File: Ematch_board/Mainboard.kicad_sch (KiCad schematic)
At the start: 72 parts, among them J10 Conn_01x02_Male, J7 RBUS, J8 USB_C_Receptacle_USB2.0, J9 Conn_01x02_Male, Q1 MMDT2222A, U2 LTC4411, U3 RT9025-25GSP, U4 LTC4411, U5 SN65HVD230, U6 INTERFACE-CP2102-GMR(QFN28)

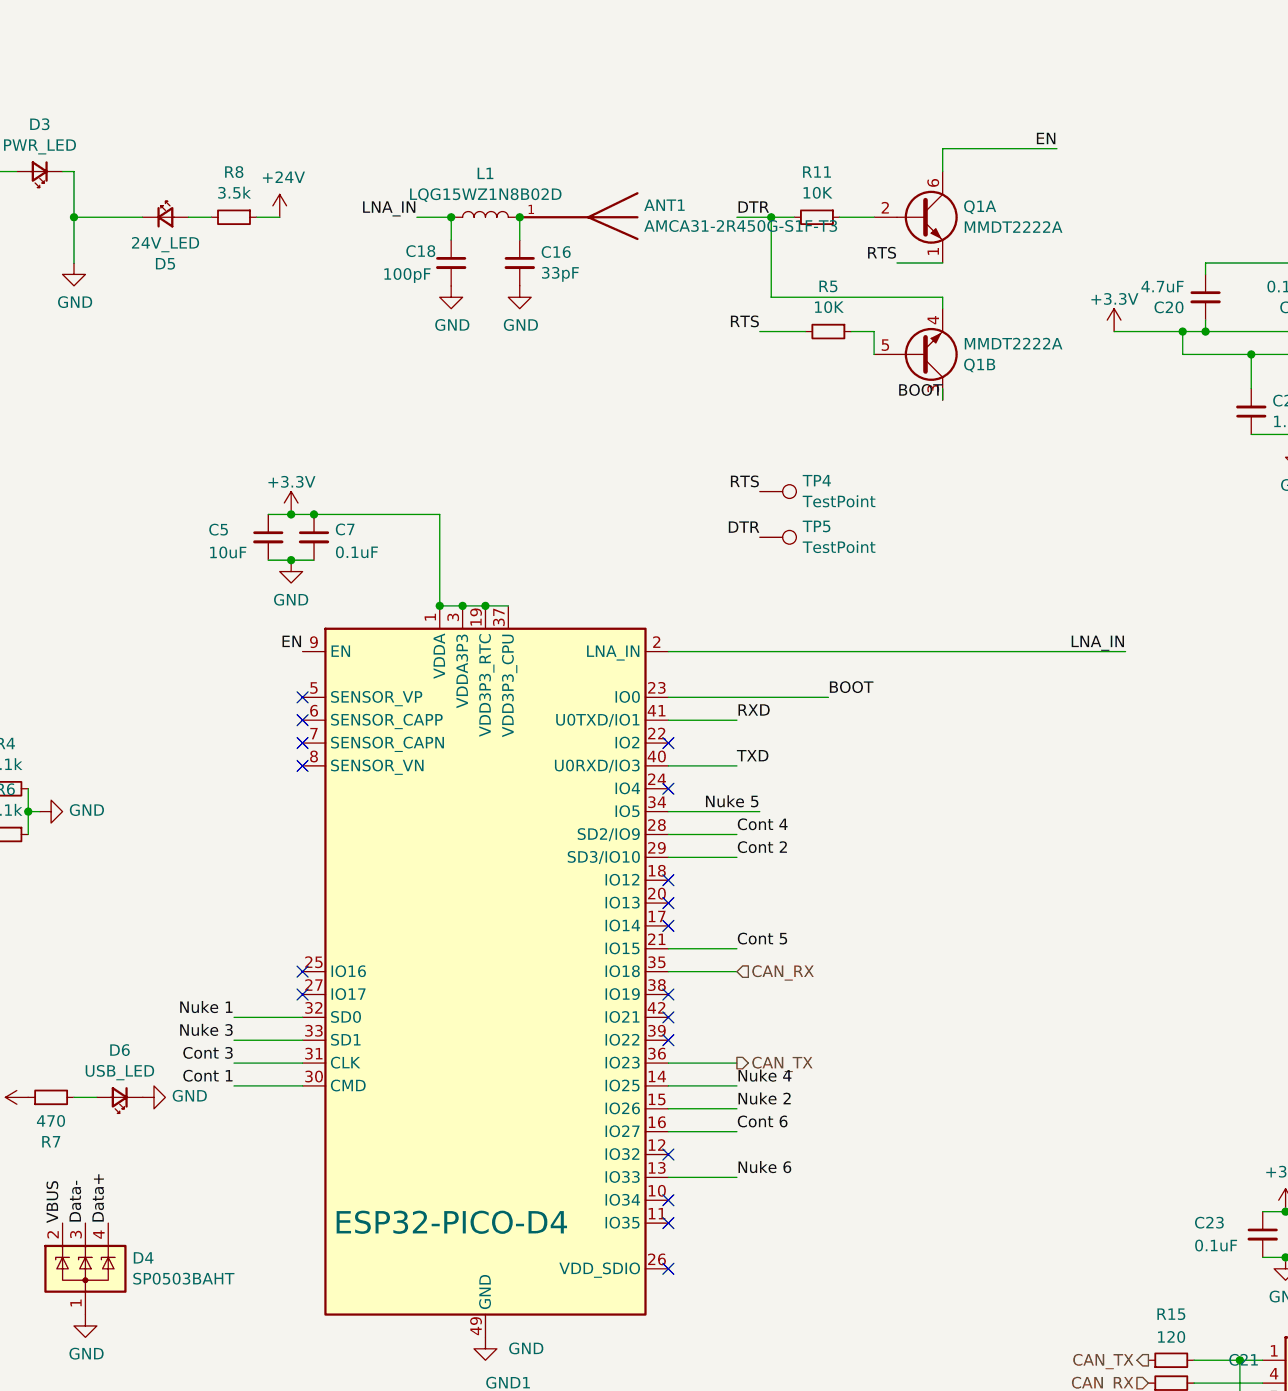
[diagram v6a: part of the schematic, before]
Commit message: completed routing, changed antenna for U.FL connector
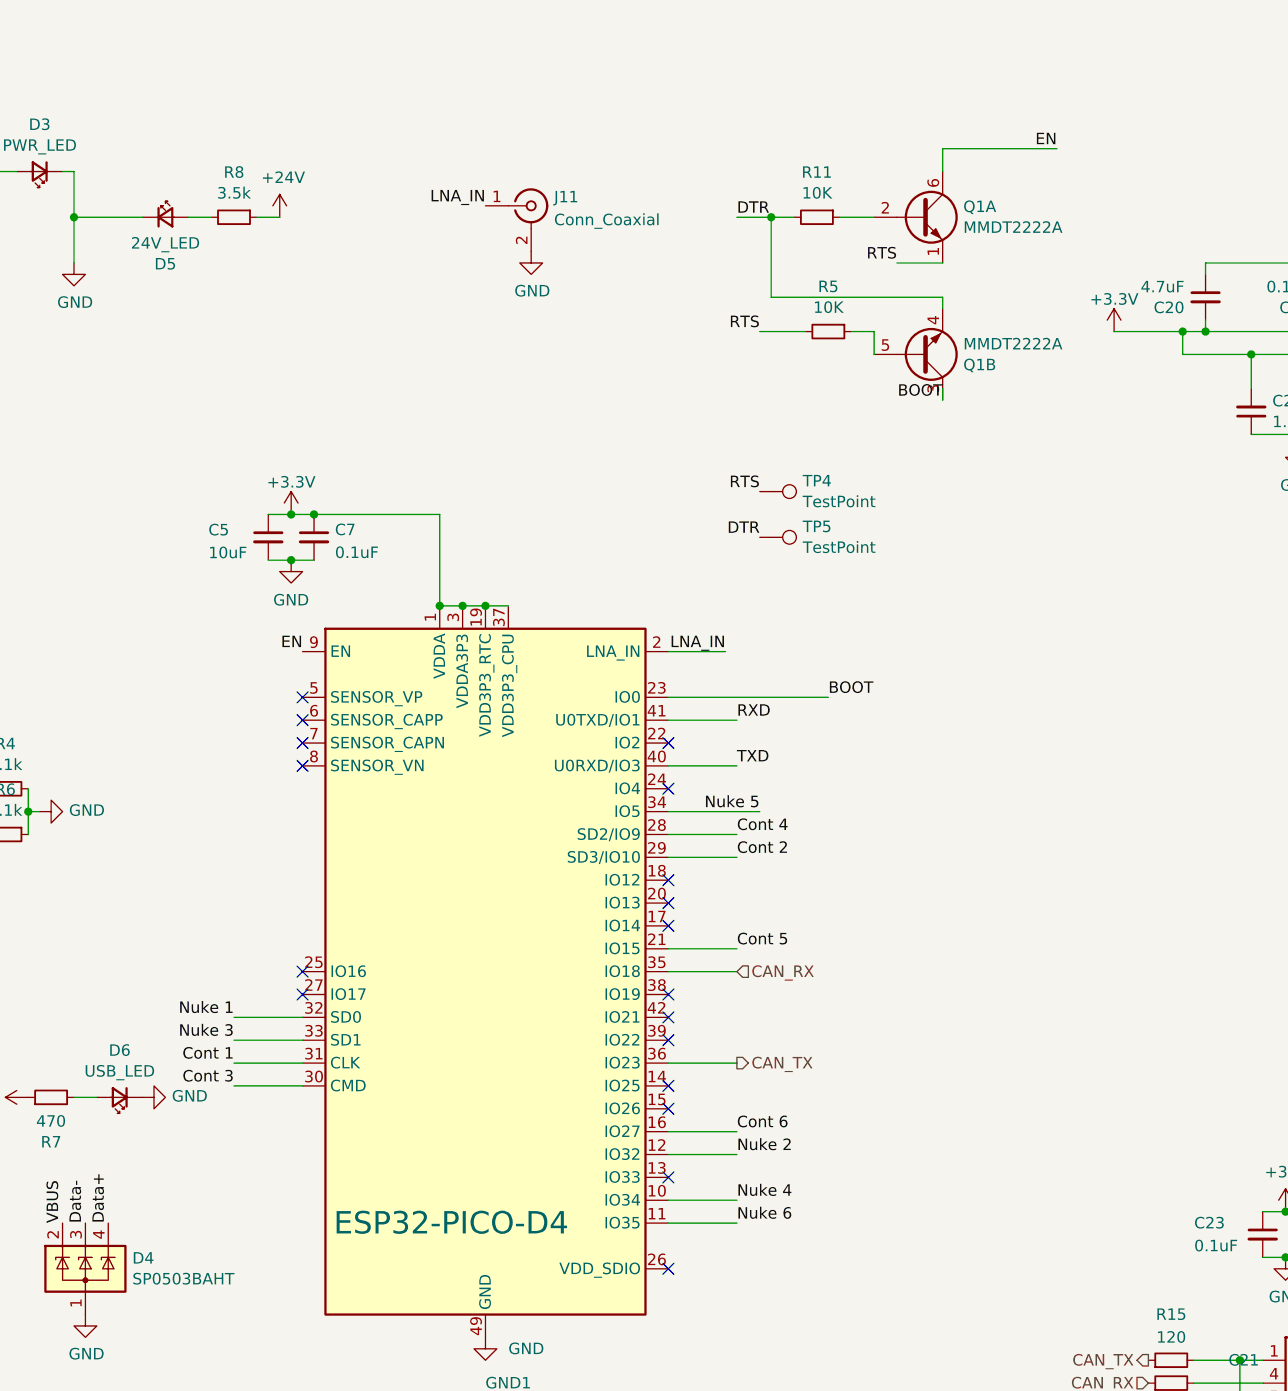
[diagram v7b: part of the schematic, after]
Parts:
- removed ANT1: AMCA31-2R450G-S1F-T3, iclr:ANT_AMCA31-2R450G-S1F-T3, symbol iclr:AMCA31-2R450G-S1F-T3
- removed C16: 33pF, Capacitor_SMD:C_0603_1608Metric, symbol Device:C_Small
- removed C18: 100pF, Capacitor_SMD:C_0603_1608Metric, symbol Device:C_Small
- removed L1: LQG15WZ1N8B02D, Inductor_SMD:L_0603_1608Metric_Pad1.05x0.95mm_HandSolder, symbol Device:L
- added J11: Conn_Coaxial, Connector_Coaxial:U.FL_Molex_MCRF_73412-0110_Vertical, symbol Connector:Conn_Coaxial
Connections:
- net Cont 1: now also GND1.31 (CLK); no longer GND1.30 (CMD)
- net Cont 3: now also GND1.30 (CMD); no longer GND1.31 (CLK)
- net GND: now also J11.2 (Ext)
- net LNA_IN: now also J11.1 (In)
- net Nuke 2: now also GND1.12 (IO32); no longer GND1.15 (IO26)
- net Nuke 4: now also GND1.10 (IO34); no longer GND1.14 (IO25)
- net Nuke 6: now also GND1.11 (IO35); no longer GND1.13 (IO33)

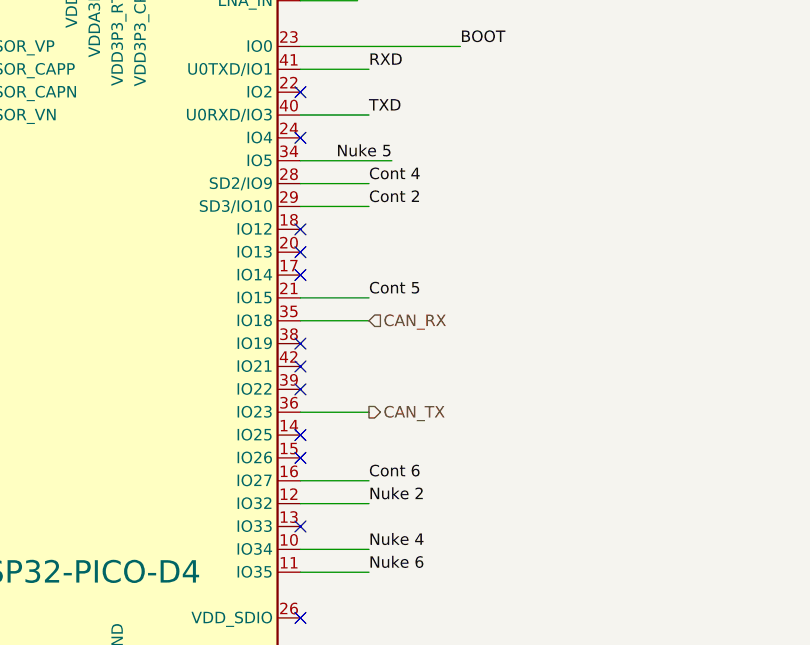
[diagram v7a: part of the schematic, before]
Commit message: created GND planes and fixed zone priority to prevent shorting nets
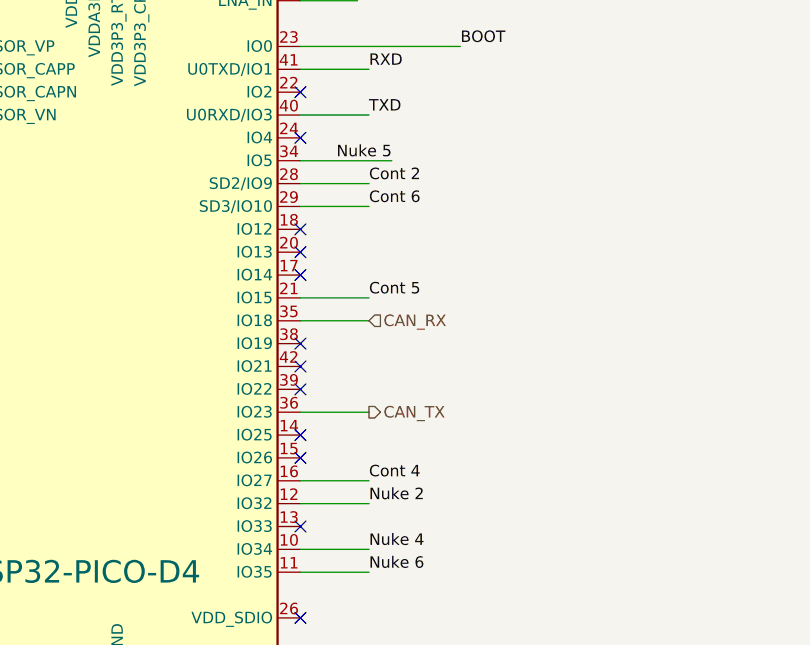
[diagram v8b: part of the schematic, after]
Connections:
- net Cont 2: now also GND1.28 (SD2/IO9); no longer GND1.29 (SD3/IO10)
- net Cont 4: now also GND1.16 (IO27); no longer GND1.28 (SD2/IO9)
- net Cont 6: now also GND1.29 (SD3/IO10); no longer GND1.16 (IO27)
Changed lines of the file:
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@@
-    (effects (font (size 1.27 1.27)) (justify left bottom))
-  )
-  (label "Cont 2" (at 132.08 93.98 0)
     (effects (font (size 1.27 1.27)) (justify left bottom))
   )
@@
     (effects (font (size 1.27 1.27)) (justify right bottom))
   )
+  (label "Cont 6" (at 132.08 93.98 0)
+    (effects (font (size 1.27 1.27)) (justify left bottom))
+  )
   (label "Cont 1" (at 76.2 116.84 180)
     (effects (font (size 1.27 1.27)) (justify right bottom))
@@
   )
   (label "Cont 6" (at 236.22 114.3 0)
-    (effects (font (size 1.27 1.27)) (justify left bottom))
-  )
-  (label "Cont 4" (at 132.08 91.44 0)
     (effects (font (size 1.27 1.27)) (justify left bottom))
   )
@@
   )
   (label "Cont 4" (at 236.22 104.14 0)
-    (effects (font (size 1.27 1.27)) (justify left bottom))
-  )
-  (label "Cont 6" (at 132.08 124.46 0)
     (effects (font (size 1.27 1.27)) (justify left bottom))
   )
@@
     (effects (font (size 1.27 1.27)) (justify left bottom))
   )
+  (label "Cont 4" (at 132.08 124.46 0)
+    (effects (font (size 1.27 1.27)) (justify left bottom))
+  )
   (label "CAN_HIGH" (at 24.13 149.86 270)
     (effects (font (size 1.27 1.27)) (justify right bottom))
@@
     (effects (font (size 1.27 1.27)) (justify left bottom))
   )
+  (label "Cont 2" (at 132.08 91.44 0)
+    (effects (font (size 1.27 1.27)) (justify left bottom))
+  )
